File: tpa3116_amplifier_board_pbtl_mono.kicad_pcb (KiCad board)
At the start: 2 copper layers, 63.5 x 50.8 mm, 47 parts, among them IC1 TPA3116D2QDADRQ1, J1 power_supply, J2 Conn_01x04, J3 power_supply, J4 output_right

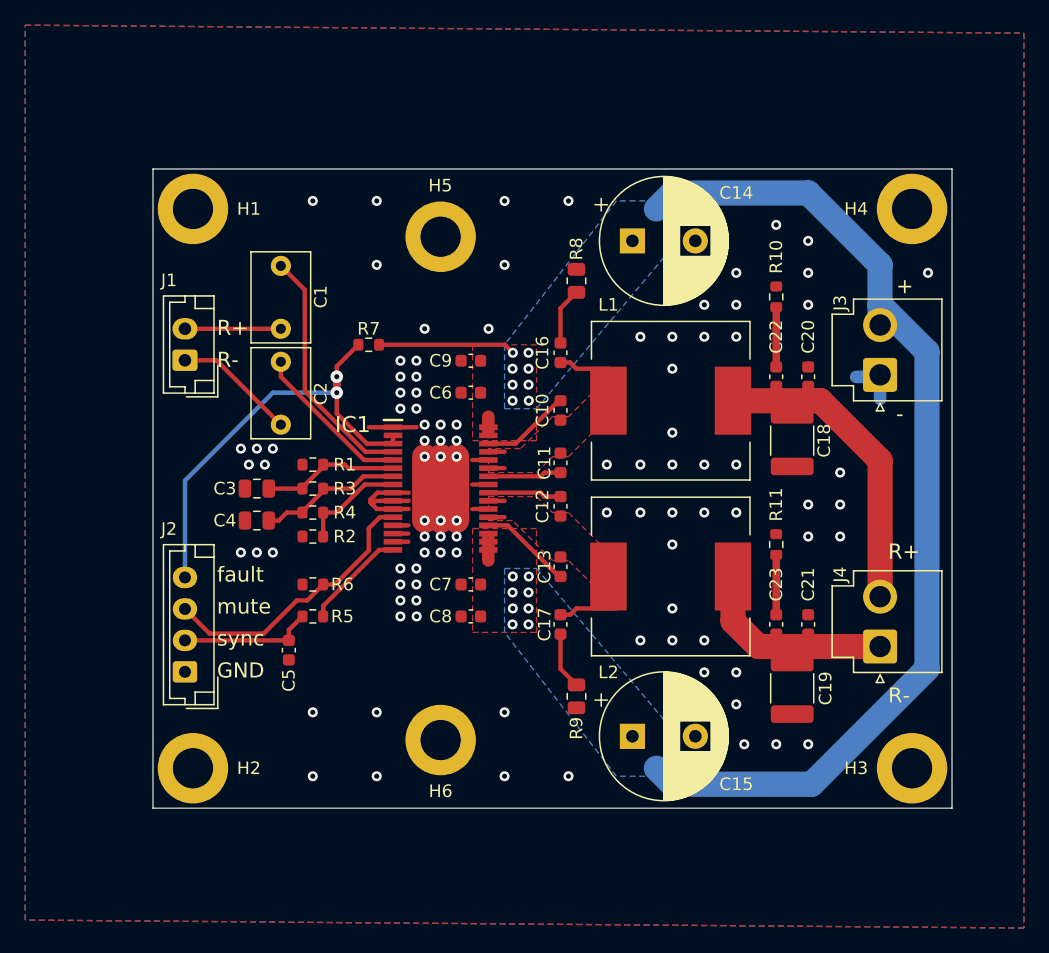
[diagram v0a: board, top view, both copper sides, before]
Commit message: Подправил дорожки и расположение R8, R9, отодвинул назад C14, C15
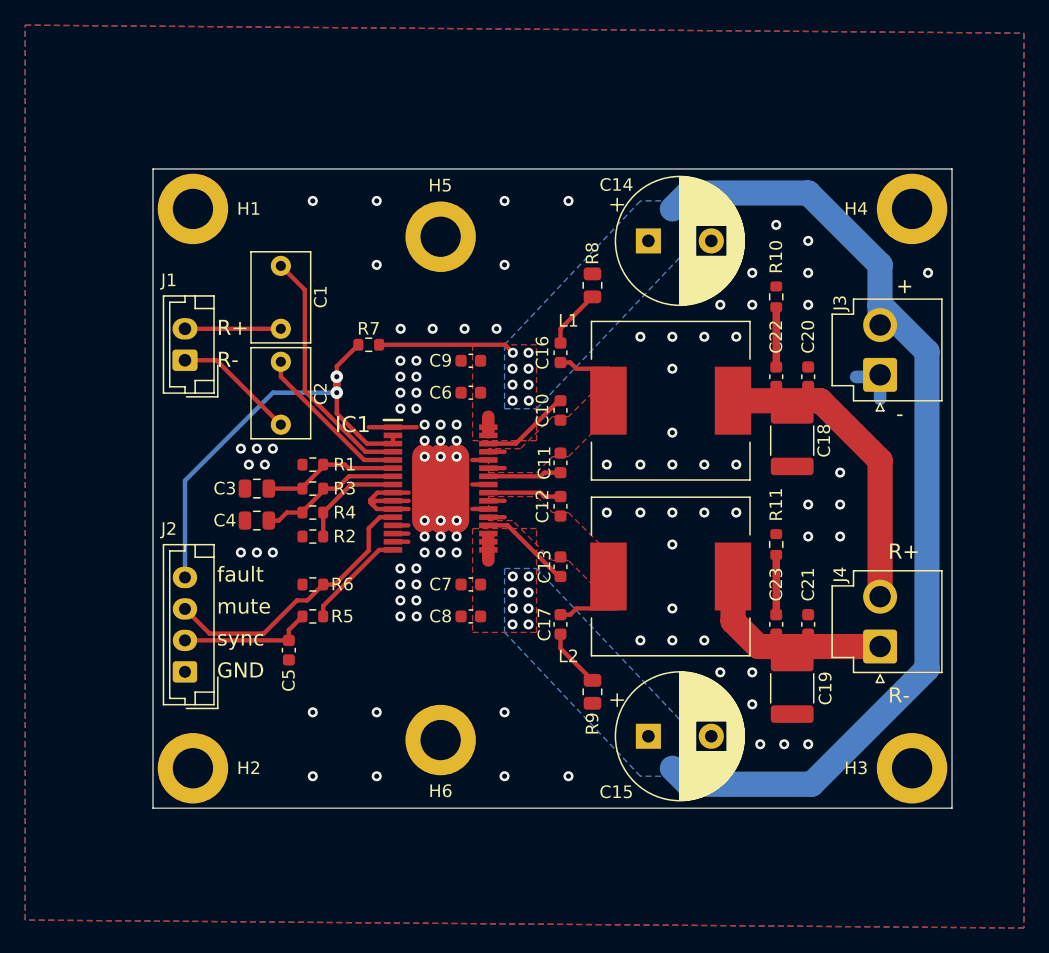
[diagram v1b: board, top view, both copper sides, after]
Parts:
- moved R9 1.32 mm to (136.5, 136.2)
- moved R8 1.32 mm to (136.5, 103.9)
- moved C14 1.27 mm to (141.0, 100.3)
- moved C15 1.27 mm to (141.0, 139.7)
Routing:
- net VCC: track 95.8 -> 93.2 mm
- net GND: vias 97 -> 99

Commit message: заменил конденсаторы C1, С2 на smd
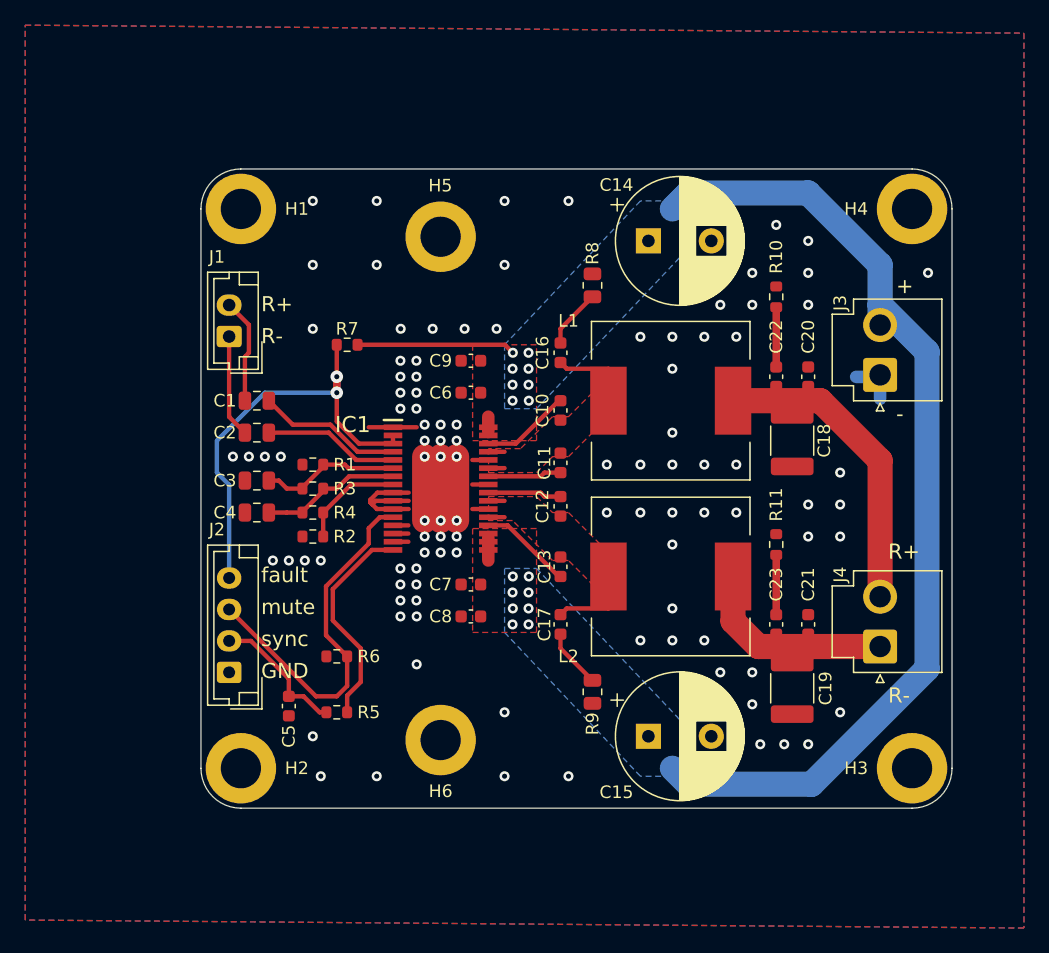
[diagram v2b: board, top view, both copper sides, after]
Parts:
- C1, C2: footprint Capacitor_THT:C_Rect_L7.0mm_W4.5mm_P5.00mm -> Capacitor_SMD:C_0805_2012Metric
- moved R5 7.85 mm to (116.2, 137.8)
- moved C1 6.02 mm to (109.9, 113.0), turned to 0 degrees
- moved R6 6.02 mm to (116.2, 133.3)
- moved C5 4.45 mm to (112.4, 137.3)
- moved J1 3.98 mm to (107.7, 107.9)
- moved H1 3.81 mm to (108.6, 97.8)
- moved H2 3.81 mm to (108.6, 142.2)
- moved J2 3.51 mm to (107.7, 134.6)
- moved C2 2.01 mm to (109.9, 115.6), turned to 0 degrees
- moved R7 1.72 mm to (117.0, 108.6)
- moved C3 0.64 mm to (109.9, 119.4)
- moved C4 0.64 mm to (109.9, 121.9)
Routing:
- net Net-(IC1-SYNC): track 8.23 -> 17.2 mm
- net Net-(IC1-RINP): track 19.7 -> 11.5 mm
- net /mute: track 22.2 -> 29.5 mm
- net Net-(IC1-RINN): track 12.8 -> 10.8 mm
- net Net-(IC1-OUTNL): track 7.23 -> 9.14 mm
- net VCC: track 93.2 -> 94.9 mm
- net /R-: track 9.74 -> 8.16 mm
- net /R+: track 7.62 -> 8.38 mm
- net /SD_LR: track 36.2 -> 35.6 mm
- net GND: vias 99 -> 102
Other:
- board size 63.5 x 50.8 mm -> 59.7 x 50.8 mm

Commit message: изменил номинал конденсатора C3
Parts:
- C3: value 1u -> --
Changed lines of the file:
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@@
         (effects (font (size 1 1) (thickness 0.15)))
     )
-    (fp_text value "1u" (at 0 1.68) (layer "F.Fab")
+    (fp_text value "--" (at 0 1.68) (layer "F.Fab")
         (effects (font (size 1 1) (thickness 0.15)))
     )

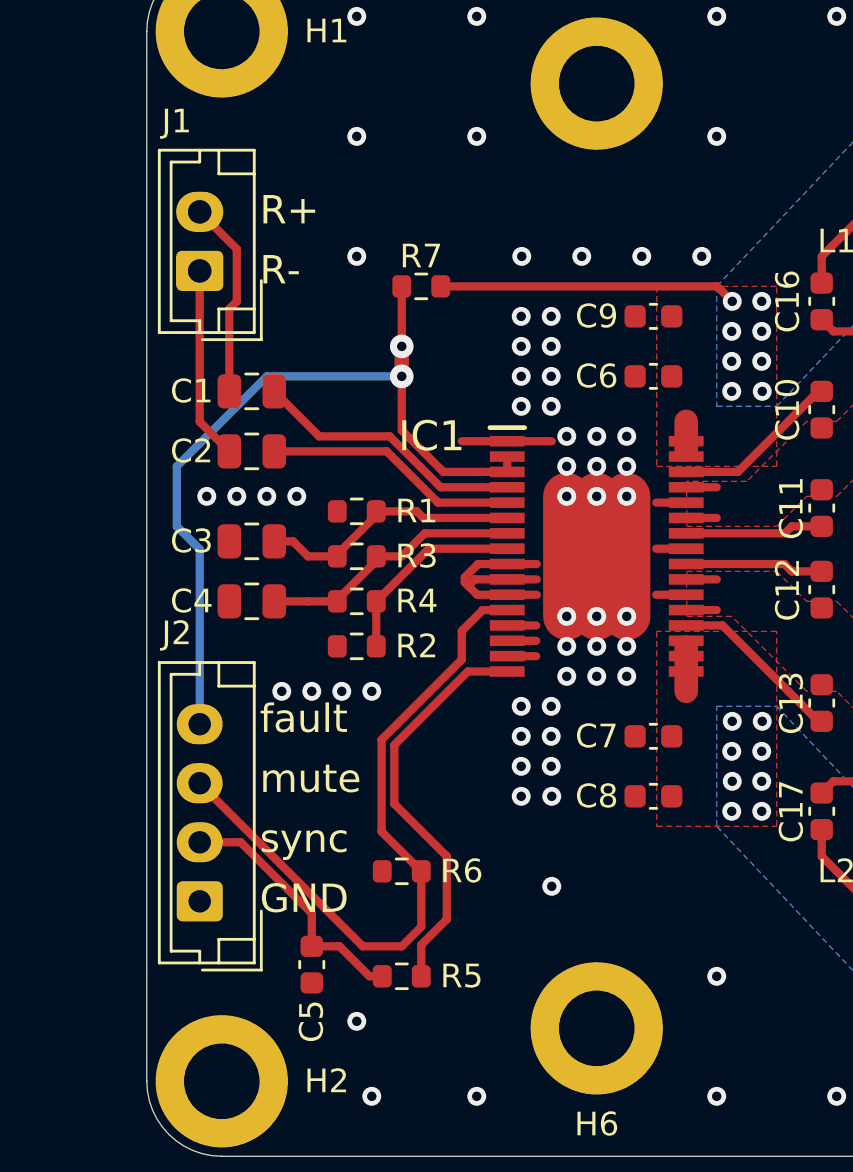
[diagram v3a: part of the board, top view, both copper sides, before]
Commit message: Перевернул входные разъемы, изменил номинал конденсаторов входных
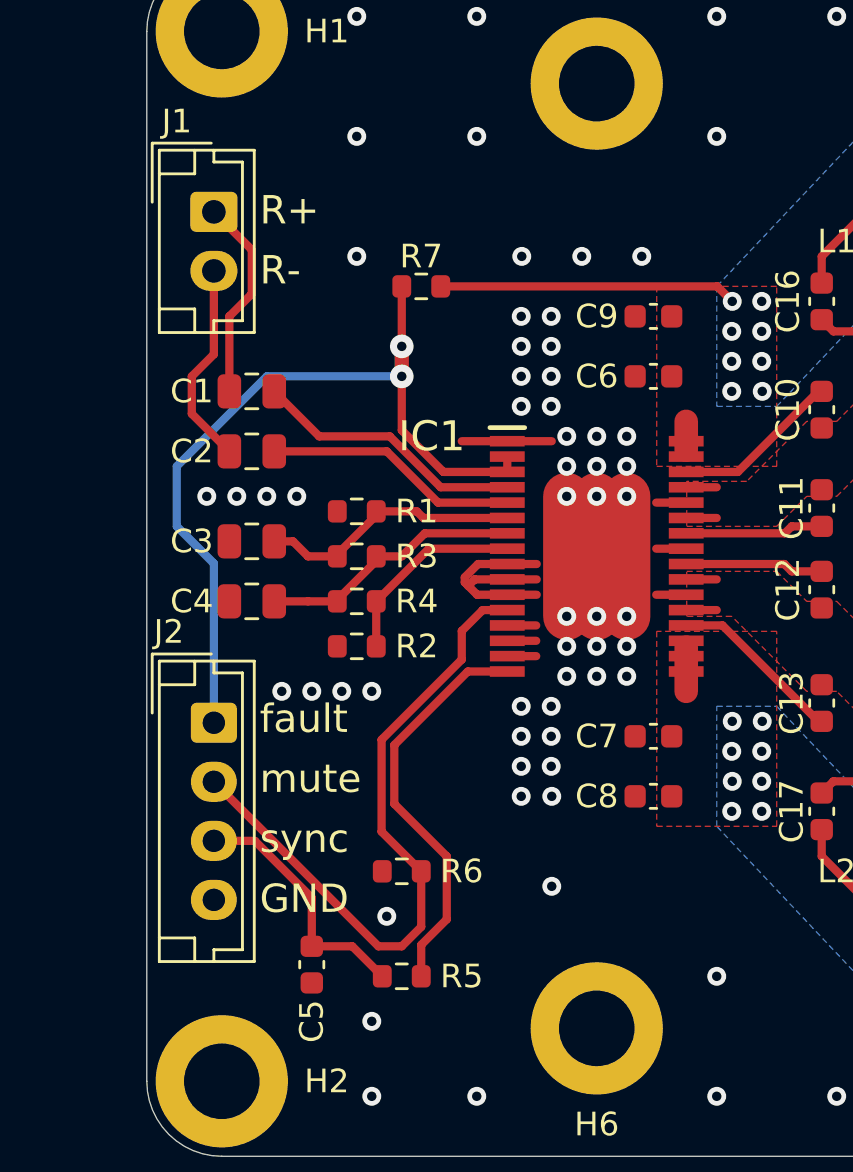
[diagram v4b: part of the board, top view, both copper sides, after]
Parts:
- C1, C2: value 470n -> 2.2u
- C18, C19: value 470n -> 680n
- C5: value 330p -> 47p
- moved J2 7.58 mm to (108.2, 127.1), turned to -90 degrees
- moved J1 2.57 mm to (108.2, 105.4), turned to -90 degrees
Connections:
- J1 pad 1: /R- -> /R+
- J1 pad 2: /R+ -> /R-
- J2 pad 1: GND -> /SD_LR
- J2 pad 2: /sync -> /mute
- J2 pad 3: /mute -> /sync
- J2 pad 4: /SD_LR -> GND
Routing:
- net /mute: track 29.5 -> 28.8 mm
- net /R-: track 8.16 -> 8.69 mm

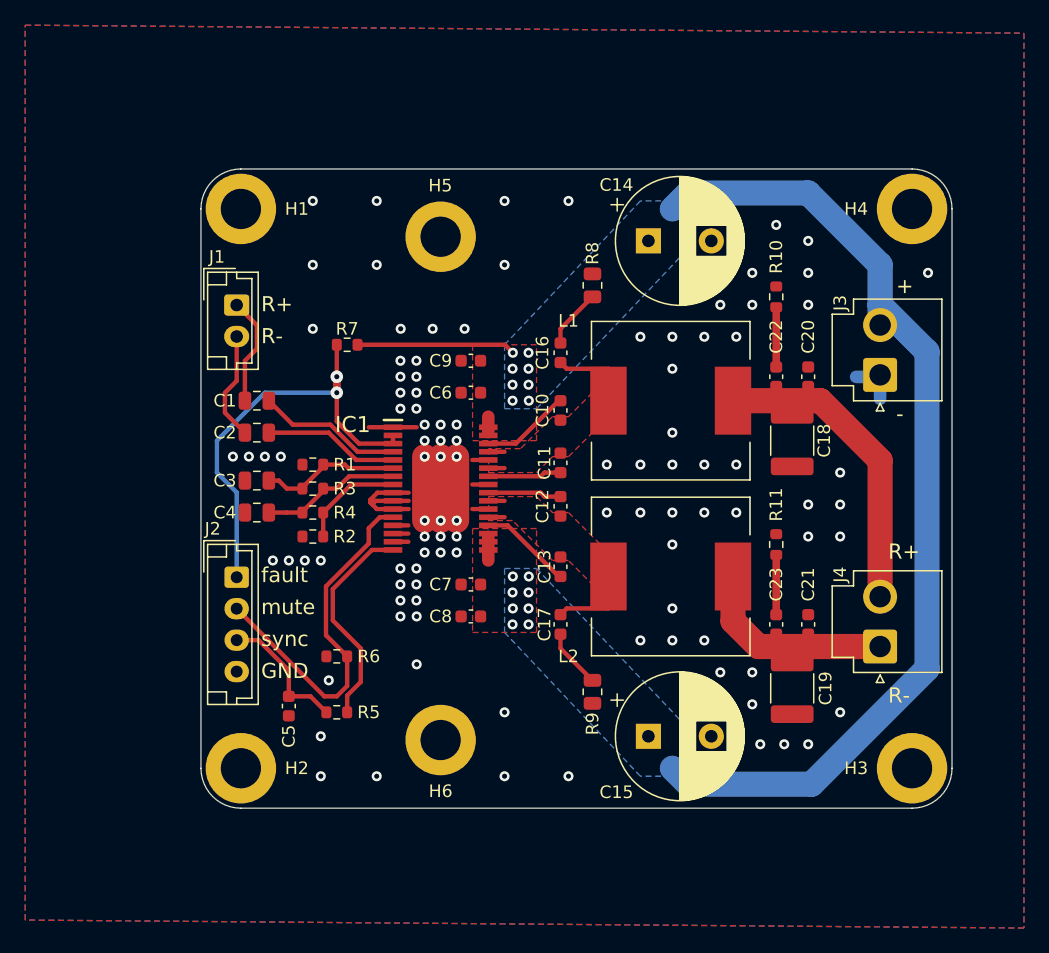
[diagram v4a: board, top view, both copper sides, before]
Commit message: заменил входные разъемы на PH 2.0
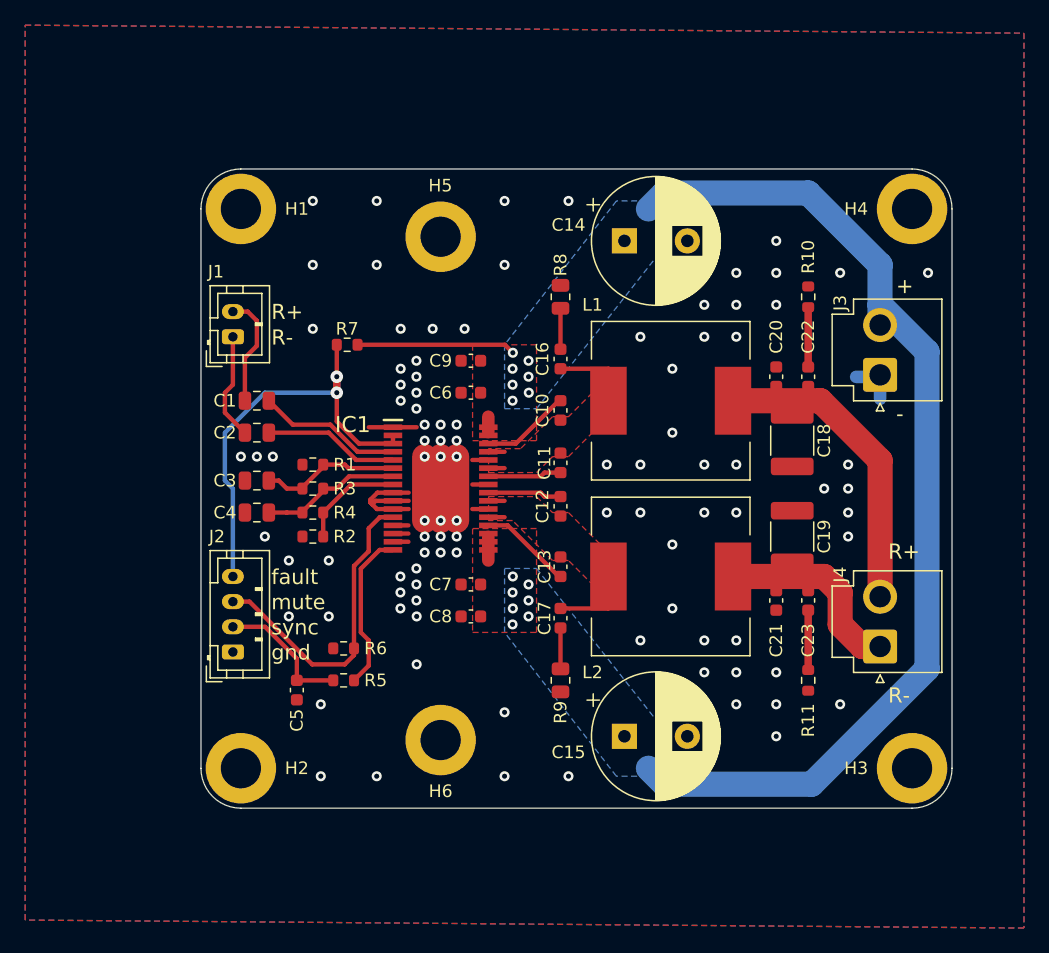
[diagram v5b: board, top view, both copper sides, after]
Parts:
- J1: footprint Connector_JST:JST_EH_B2B-EH-A_1x02_P2.50mm_Vertical -> Connector_JST:JST_PH_B2B-PH-K_1x02_P2.00mm_Vertical
- J2: footprint Connector_JST:JST_EH_B4B-EH-A_1x04_P2.50mm_Vertical -> Connector_JST:JST_PH_B4B-PH-K_1x04_P2.00mm_Vertical
- moved C19 12.1 mm to (152.4, 123.8), turned to 90 degrees
- moved R11 11.1 mm to (153.7, 135.3), turned to 90 degrees
- moved J2 5.95 mm to (108.0, 133.0), turned to 90 degrees
- moved C23 3.18 mm to (153.7, 128.9), turned to -90 degrees
- moved C21 3.17 mm to (151.1, 128.9), turned to -90 degrees
- moved R8 2.70 mm to (134.0, 104.8)
- moved R9 2.70 mm to (134.0, 135.3)
- moved R5 2.60 mm to (116.8, 135.3)
- moved C20 2.54 mm to (151.1, 111.1)
- moved C22 2.54 mm to (153.7, 111.1)
- moved R10 2.54 mm to (153.7, 104.8)
- moved J1 2.54 mm to (108.0, 108.0), turned to 90 degrees
- moved C14 1.91 mm to (139.1, 100.3)
- moved C15 1.91 mm to (139.1, 139.7)
- moved C5 1.42 mm to (113.0, 136.0)
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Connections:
- J1 pad 1: /R+ -> /R-
- J1 pad 2: /R- -> /R+
- J2 pad 1: /SD_LR -> GND
- J2 pad 2: /mute -> /sync
- J2 pad 3: /sync -> /mute
- J2 pad 4: GND -> /SD_LR
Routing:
- net Net-(IC1-SYNC): track 17.2 -> 12.8 mm
- net /mute: track 28.8 -> 24.8 mm
- net VCC: track 94.9 -> 98.7 mm, vias 16 -> 14
- net Net-(C17-Pad2): track 4.72 -> 3.25 mm
- net Net-(C16-Pad2): track 4.72 -> 3.25 mm
- net Net-(J4-Pin_1): track 16.1 -> 15.5 mm
- net /SD_LR: track 35.9 -> 35.4 mm
- net GND: vias 102 -> 96
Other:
- board text added: "gnd"
- board text removed: "GND"
